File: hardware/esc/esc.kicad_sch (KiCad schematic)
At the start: 58 parts, among them J1 TO_FC, J2 BAT_IN, J3 BAT_GND, U1 TPS563200, U2 NCP59800BMNADJTAG

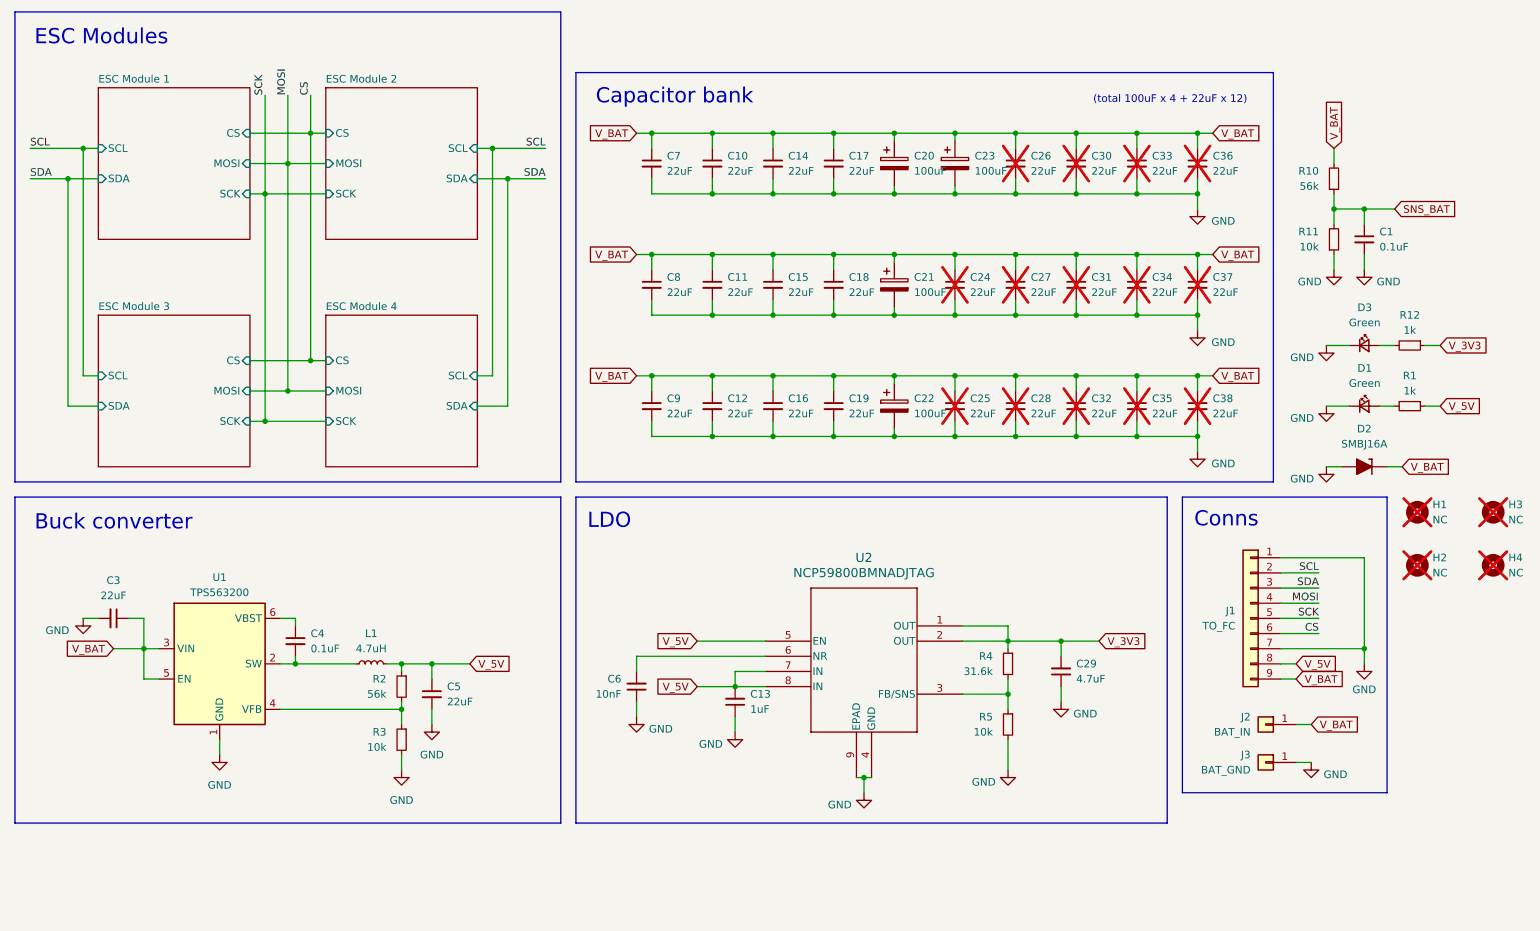
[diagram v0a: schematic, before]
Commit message: h/fix: separate power into a separate sheet; send to fab
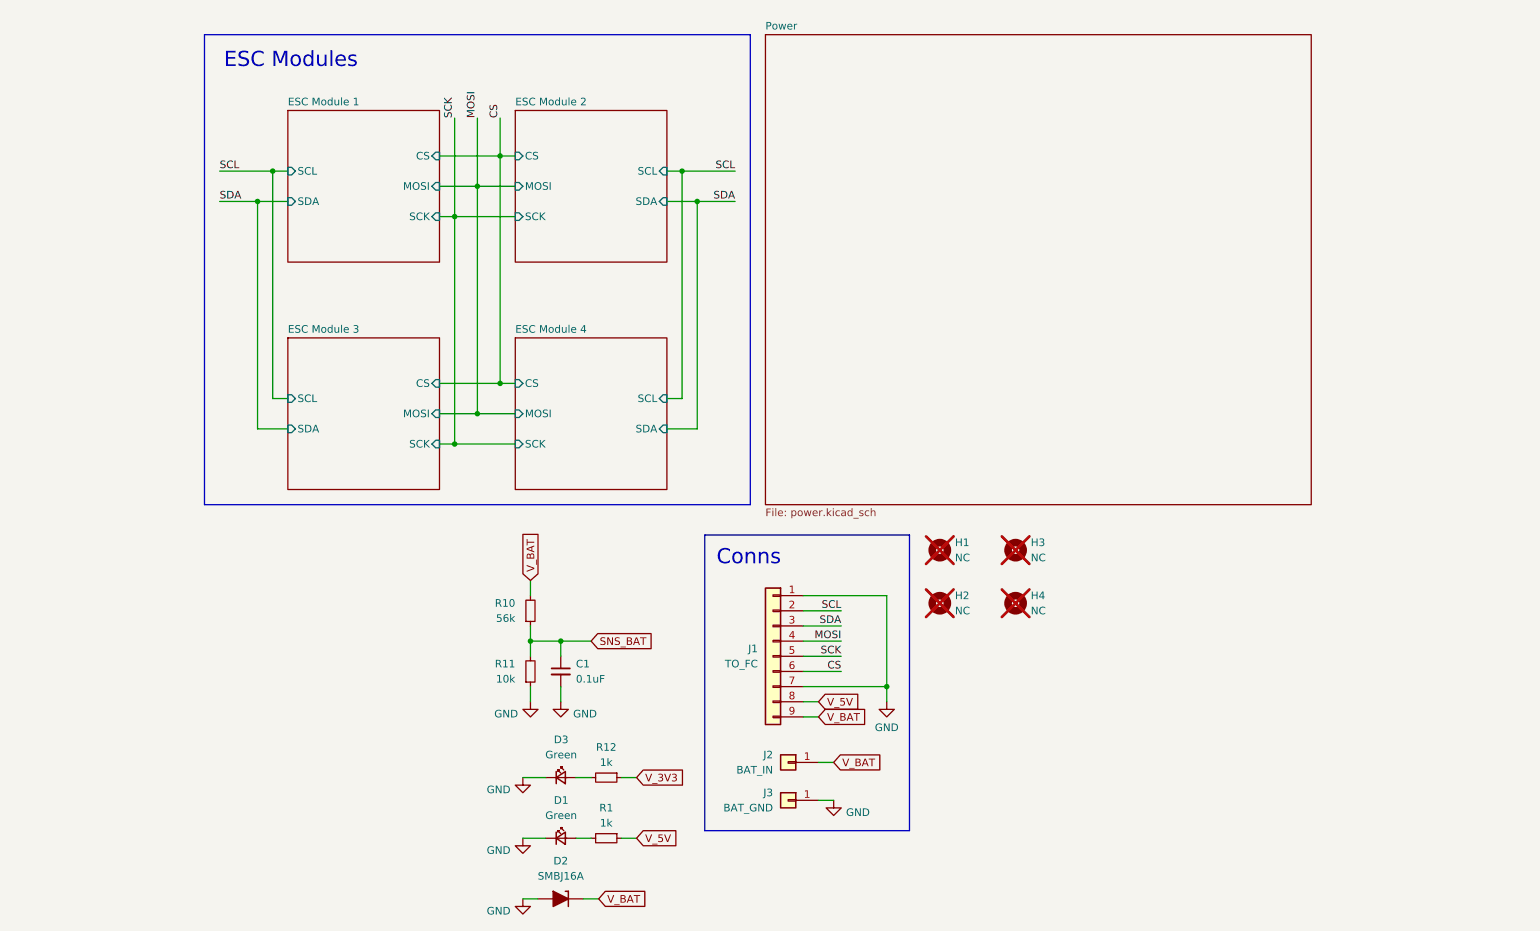
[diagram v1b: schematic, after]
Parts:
- removed C10, C11, C12, C14, C15, C16, C17, C18, C19, C24, C25, C26, C27, C28, C3, C30, C31, C32, C33, C34, C35, C36, C37, C38, C5, C7, C8, C9: 22uF, Capacitor_SMD:C_0805_2012Metric, symbol Device:C_Small
- removed C13: 1uF, Capacitor_SMD:C_0402_1005Metric, symbol Device:C_Small
- removed C20, C21, C22, C23: 100uF, Stratus:ECASD61C107M012KA0, symbol Device:C_Polarized
- removed C29: 4.7uF, Capacitor_SMD:C_0603_1608Metric, symbol Device:C_Small
- removed C4: 0.1uF, Capacitor_SMD:C_0402_1005Metric, symbol Device:C_Small
- removed C6: 10nF, Capacitor_SMD:C_0402_1005Metric, symbol Device:C_Small
- removed L1: 4.7uH, Inductor_SMD:L_Taiyo-Yuden_MD-4040, symbol Device:L_Small
- removed R2: 56k, Resistor_SMD:R_0402_1005Metric, symbol Device:R_Small
- removed R3, R5: 10k, Resistor_SMD:R_0402_1005Metric, symbol Device:R_Small
- removed R4: 31.6k, Resistor_SMD:R_0402_1005Metric, symbol Device:R_Small
- removed U1: TPS563200, Stratus:TPS563200, symbol Regulator_Switching:TPS563200
- removed U2: NCP59800BMNADJTAG, Stratus:NCP59800BMNADJTAG, symbol NCP59800BMNADJTAG:NCP59800BMNADJTAG
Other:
- added sheet Power (power.kicad_sch)
- note removed: "(total 100uF x 4 + 22uF x 12)"
- note removed: "Buck converter"
- note removed: "Capacitor bank"
- note removed: "LDO"
- moved on the sheet: C1, D1, D2, D3, H1, H2, H3, H4, J1, J2, J3, R1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

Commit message: h/feat: preliminary rev 2 schematic
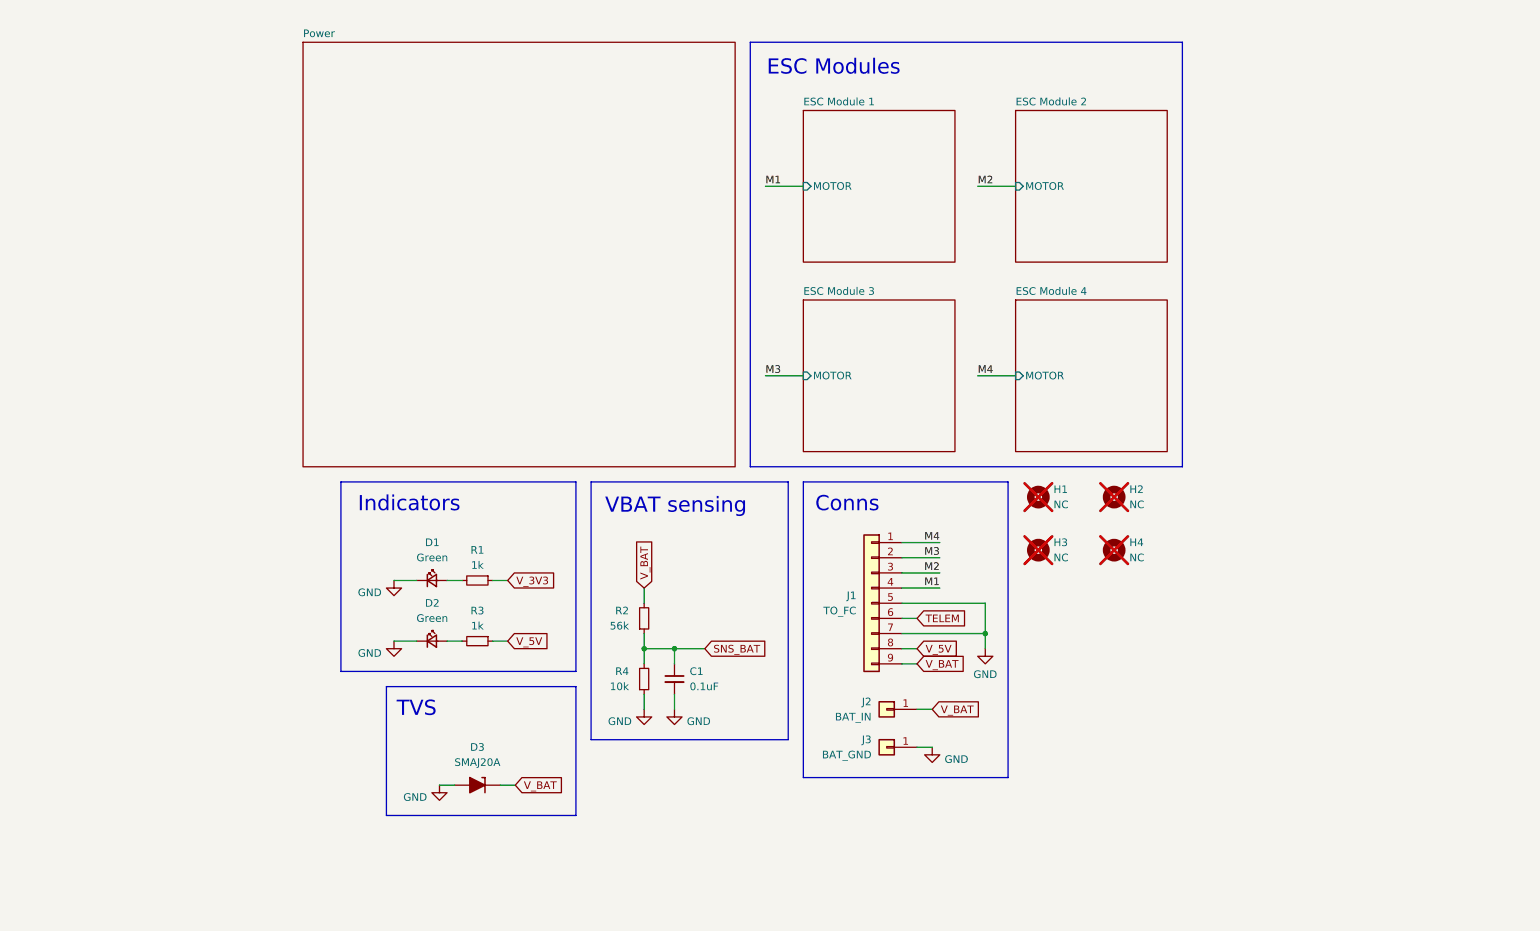
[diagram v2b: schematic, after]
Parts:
- D3: renamed from D2; value SMBJ16A -> SMAJ20A
- renumbered D3 to D1, D1 to D2, H3 to H2, H2 to H3, R12 to R1, R10 to R2, R1 to R3, R11 to R4
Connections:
- net SCK is gone; now on net GND: J1.5 (Pin_5)
- net GND: no longer J1.1 (Pin_1)
- net CS renamed TELEM
- net MOSI renamed M1
- net SCL renamed M3
- net SDA renamed M2
- new net M4: J1.1 (Pin_1)
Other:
- sheet ESC Module 1 ports: added MOTOR; removed CS, MOSI, SCK, SCL, SDA
- sheet ESC Module 2 ports: added MOTOR; removed CS, MOSI, SCK, SCL, SDA
- sheet ESC Module 3 ports: added MOTOR; removed CS, MOSI, SCK, SCL, SDA
- sheet ESC Module 4 ports: added MOTOR; removed CS, MOSI, SCK, SCL, SDA
- note added: "Indicators"
- note added: "TVS"
- note added: "VBAT sensing"
- moved on the sheet: C1, D1, D2, D3, H1, H2, H3, H4, J1, J2, J3, R1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

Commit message: chore: prep: footprints, 3d models, pcb
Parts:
- removed D3: SMAJ20A, Stratus:SMBJ10A, symbol PCM_Diode_TVS_AKL:SMBJ10A
- added D3: SMAJ20A, Stratus:SMAJ20A, symbol Diode:SMAJ20A
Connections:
- net GND: now also D3.2 (A2)
- net V_BAT: now also D3.1 (A1)
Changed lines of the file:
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@@
 	)
 	(symbol
-		(lib_id "PCM_Diode_TVS_AKL:SMBJ10A")
-		(at 101.6 157.48 0)
+		(lib_id "Diode:SMAJ20A")
+		(at 101.6 157.48 180)
 		(unit 1)
 		(body_style 1)
@@
 			)
 		)
-		(property "Footprint" "Stratus:SMBJ10A"
-			(at 101.6 157.48 0)
+		(property "Footprint" "Stratus:SMAJ20A"
+			(at 101.6 152.4 0)
 			(hide yes)
 			(show_name no)
@@
 			)
 		)
-		(property "Datasheet" "https://www.littelfuse.com/assetdocs/tvs-diodes-smaj-datasheet?assetguid=13c2a823-03b8-4d1f-9ddc-9b44670aed9d"
-			(at 101.6 157.48 0)
+		(property "Datasheet" "https://www.littelfuse.com/media?resourcetype=datasheets&itemid=75e32973-b177-4ee3-a0ff-cedaf1abdb93&filename=smaj-datasheet"
+			(at 102.87 157.48 0)
 			(hide yes)
 			(show_name no)
@@
 			)
 		)
-		(property "Description" "SMB Unidirectional TVS diode, 10V, 600W, Alternate KiCAD Library"
+		(property "Description" "400W unidirectional Transient Voltage Suppressor, 20.0Vr, SMA(DO-214AC)"
 			(at 101.6 157.48 0)
 			(hide yes)
-			(show_name no)
-			(do_not_autoplace no)
-			(effects
-				(font
-					(size 1.27 1.27)
-				)
-			)
-		)
-		(property "Manufacturer_Name" "Littelfuse"
-			(at 101.6 157.48 0)
-			(hide yes)
-			(show_name no)
-			(do_not_autoplace no)
-			(effects
-				(font
-					(size 1.27 1.27)
-				)
-			)
-		)
-		(property "Manufacturer_Part_Number" "SMBJ16A"
-			(at 101.6 157.48 0)
-			(hide yes)

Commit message: h/feat: gate drive routing + prelim layout
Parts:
- C1: footprint Capacitor_SMD:C_0402_1005Metric -> Stratus:C_0402
- R1, R2, R3, R4: footprint Resistor_SMD:R_0402_1005Metric -> Stratus:R_0402
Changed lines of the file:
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@@
 			)
 		)
-		(property "Footprint" "Resistor_SMD:R_0402_1005Metric"
+		(property "Footprint" "Stratus:R_0402"
 			(at 101.6 133.35 0)
 			(hide yes)
@@
 			)
 		)
-		(property "Footprint" "Resistor_SMD:R_0402_1005Metric"
+		(property "Footprint" "Stratus:R_0402"
 			(at 129.54 129.54 0)
 			(hide yes)
@@
 			)
 		)
-		(property "Footprint" "Resistor_SMD:R_0402_1005Metric"
+		(property "Footprint" "Stratus:R_0402"
 			(at 101.6 123.19 0)
 			(hide yes)
@@
 			)
 		)
-		(property "Footprint" "Resistor_SMD:R_0402_1005Metric"
+		(property "Footprint" "Stratus:R_0402"
 			(at 129.54 139.7 0)
 			(hide yes)
@@
 			)
 		)
-		(property "Footprint" "Capacitor_SMD:C_0402_1005Metric"
+		(property "Footprint" "Stratus:C_0402"
 			(at 134.62 139.7 0)
 			(hide yes)

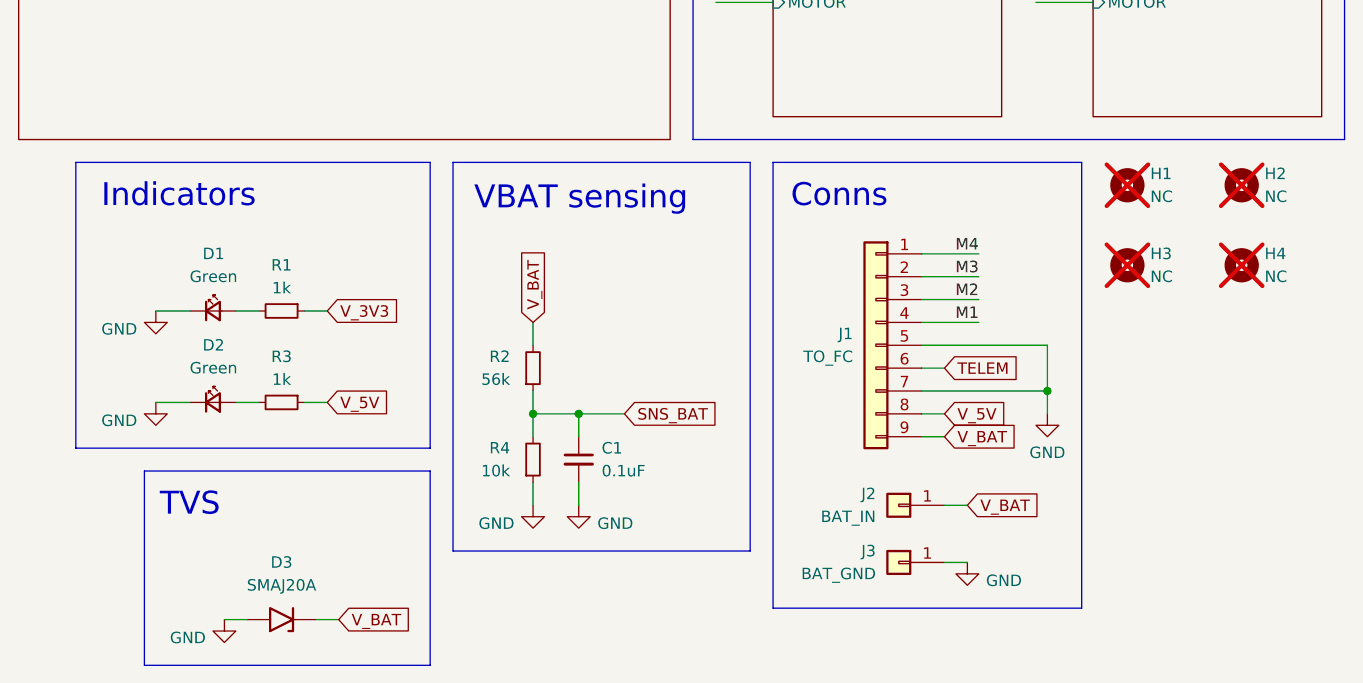
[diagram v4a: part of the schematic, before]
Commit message: h/fix: move v_bat sensing to FC
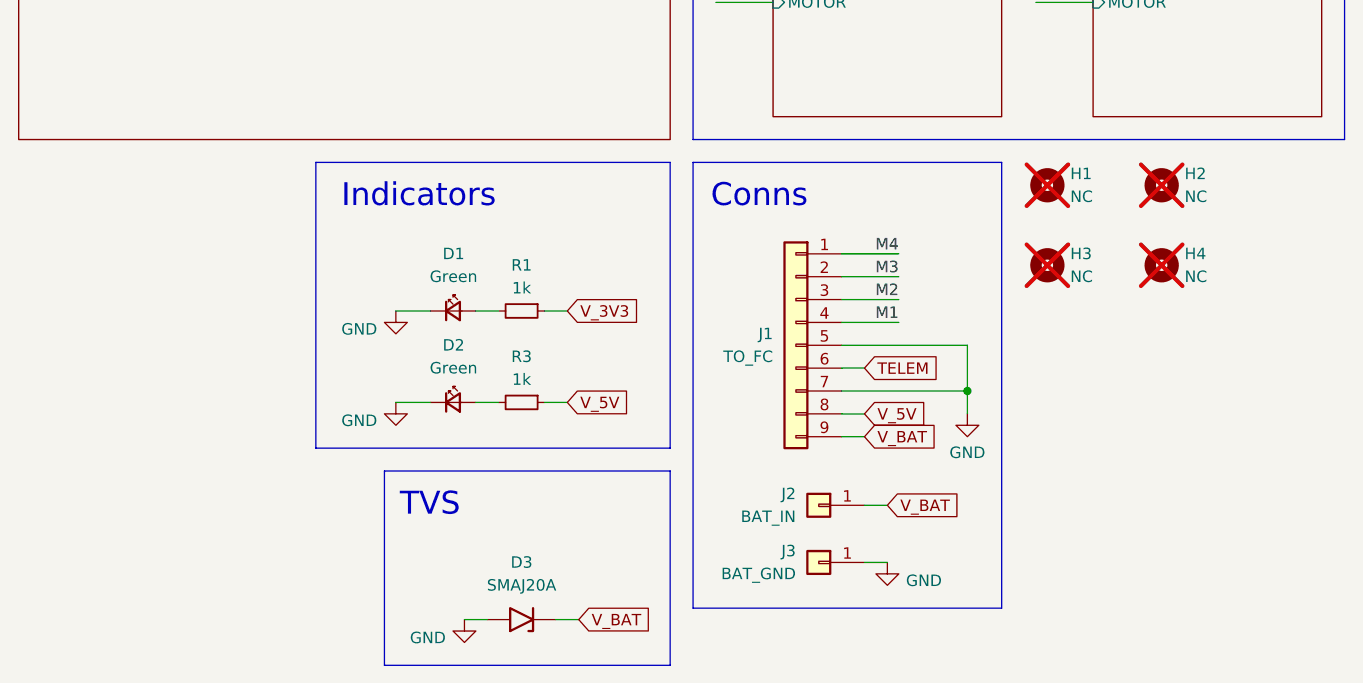
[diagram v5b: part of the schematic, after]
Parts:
- removed C1: 0.1uF, Stratus:C_0402, symbol Device:C_Small
- removed R2: 56k, Stratus:R_0402, symbol Device:R_Small
- removed R4: 10k, Stratus:R_0402, symbol Device:R_Small
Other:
- note removed: "VBAT sensing"
- moved on the sheet: D1, D2, D3, H1, H2, H3, H4, J1, J2, J3, R1, R3

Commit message: h/feat: power stage; finalise placement
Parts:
- D1, D2: footprint LED_SMD:LED_0402_1005Metric -> LED_SMD:LED_0603_1608Metric
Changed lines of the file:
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@@
 			)
 		)
-		(property "Footprint" "LED_SMD:LED_0402_1005Metric"
+		(property "Footprint" "LED_SMD:LED_0603_1608Metric"
 			(at 120.65 123.19 90)
 			(hide yes)
@@
 			)
 		)
-		(property "Footprint" "LED_SMD:LED_0402_1005Metric"
+		(property "Footprint" "LED_SMD:LED_0603_1608Metric"
 			(at 120.65 133.35 90)
 			(hide yes)

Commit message: h/feat: add vias for central mlccs
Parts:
- J2: footprint Stratus:Batt_Pad_5x5_D2.5 -> Stratus:Input_5x5_D2.5_R
- J3: footprint Stratus:Batt_Pad_5x5_D2.5 -> Stratus:Input_5x5_D2.5_L
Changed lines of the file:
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@@
 			)
 		)
-		(property "Footprint" "Stratus:Batt_Pad_5x5_D2.5"
+		(property "Footprint" "Stratus:Input_5x5_D2.5_L"
 			(at 161.29 151.13 0)
 			(hide yes)
@@
 			)
 		)
-		(property "Footprint" "Stratus:Batt_Pad_5x5_D2.5"
+		(property "Footprint" "Stratus:Input_5x5_D2.5_R"
 			(at 161.29 144.78 0)
 			(hide yes)

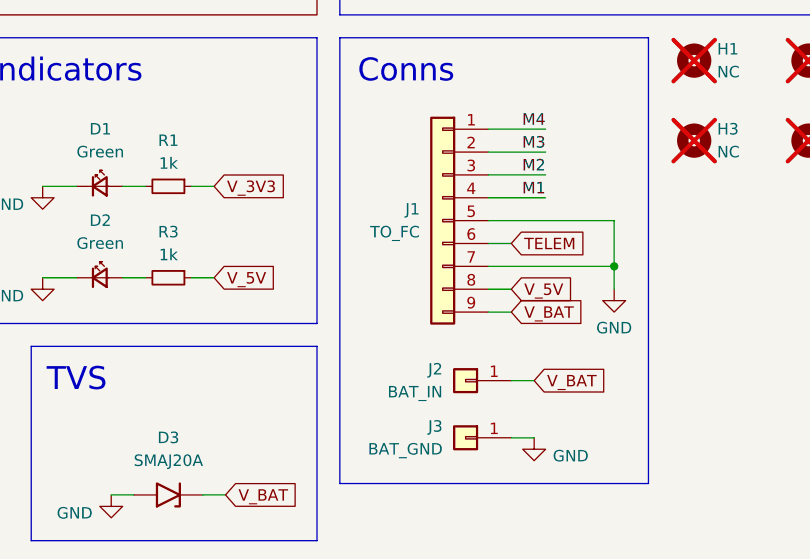
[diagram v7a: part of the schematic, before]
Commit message: h/feat: rework power stage: power drv8300 from 10v; remove 5v FC passthrough
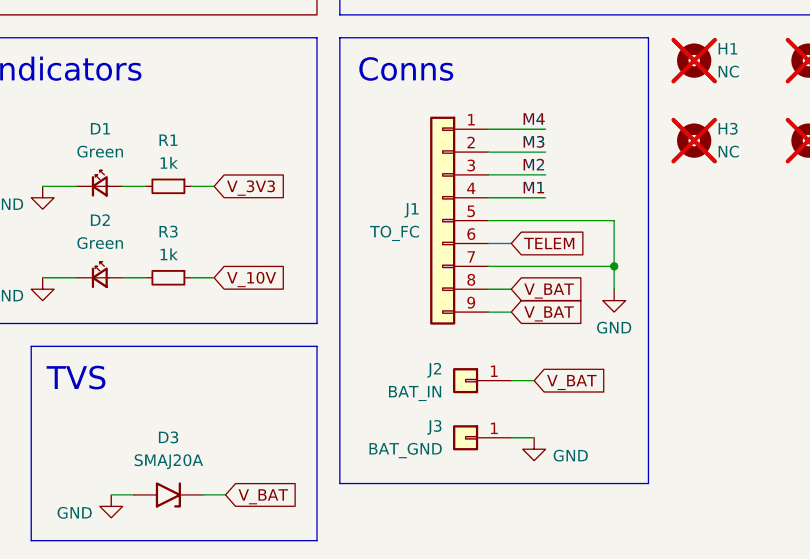
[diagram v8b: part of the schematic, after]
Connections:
- net V_BAT: now also J1.8 (Pin_8)
- net V_5V renamed V_10V
- net V_10V: no longer J1.8 (Pin_8)
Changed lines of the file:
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@@
-		)
-	)
-	(global_label "V_5V"
-		(shape input)
-		(at 166.37 134.62 0)
-		(fields_autoplaced yes)
-		(effects
-			(font
-				(size 1.27 1.27)
-			)
-			(justify left)
-		)
-		(property "Intersheetrefs" "${INTERSHEET_REFS}"
-			(at 173.7095 134.62 0)
-			(hide yes)
-			(show_name no)
-			(do_not_autoplace no)
-			(effects
-				(font
-					(size 1.27 1.27)
-				)
-				(justify left)
-			)
 		)
 	)
@@
 		)
 	)
-	(global_label "V_5V"
+	(global_label "V_10V"
 		(shape input)
 		(at 133.35 133.35 0)
@@
 		)
 		(property "Intersheetrefs" "${INTERSHEET_REFS}"
-			(at 140.6895 133.35 0)
+			(at 141.899 133.35 0)
 			(hide yes)
 			(show_name no)
+			(do_not_autoplace no)
+			(effects
+				(font
+					(size 1.27 1.27)
+				)
+				(justify left)
+			)
+		)
+	)
+	(global_label "V_BAT"
+		(shape input)
+		(at 166.37 134.62 0)
+		(fields_autoplaced yes)
+		(effects
+			(font
+				(size 1.27 1.27)
+			)
+			(justify left)
+		)
+		(property "Intersheetrefs" "${INTERSHEET_REFS}"
+			(at 174.7376 134.62 0)
+			(hide yes)
+			(show_name no)
